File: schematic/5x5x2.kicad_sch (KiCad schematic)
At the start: 180 parts, among them J1 SW Debug, J10 Conn_01x03_Female, J11 Conn_01x03_Male, J12 Conn_01x03_Male, J13 Conn_01x03_Female, J14 Conn_01x03_Female, J15 Conn_01x03_Male, J16 Conn_01x03_Female, J2 USB_C_Receptacle_USB2.0, J3 Conn_01x03_Male, J4 Conn_01x03_Male, J5 Conn_01x03_Female, J6 Conn_01x03_Female, J7 Conn_01x03_Male, J8 Conn_01x03_Male, J9 Conn_01x03_Female, SW1 SW, SW11 SW, SW12 SW, SW13 SW, SW14 SW, SW15 SW, SW21 SW, SW22 SW, SW23 SW, SW24 SW, SW25 SW, SW31 SW, SW32 SW, SW33 SW, SW34 SW, SW35 SW, SW41 SW, SW42 SW, SW43 SW, SW44 SW, SW45 SW, SW51 SW, SW52 SW, SW53 SW, SW54 SW, SW55 SW, SW6 ALPS_EC11, U1 SRV0504, U2 STM32F103C8, U3 LD1117S33CTR, Y1 16M

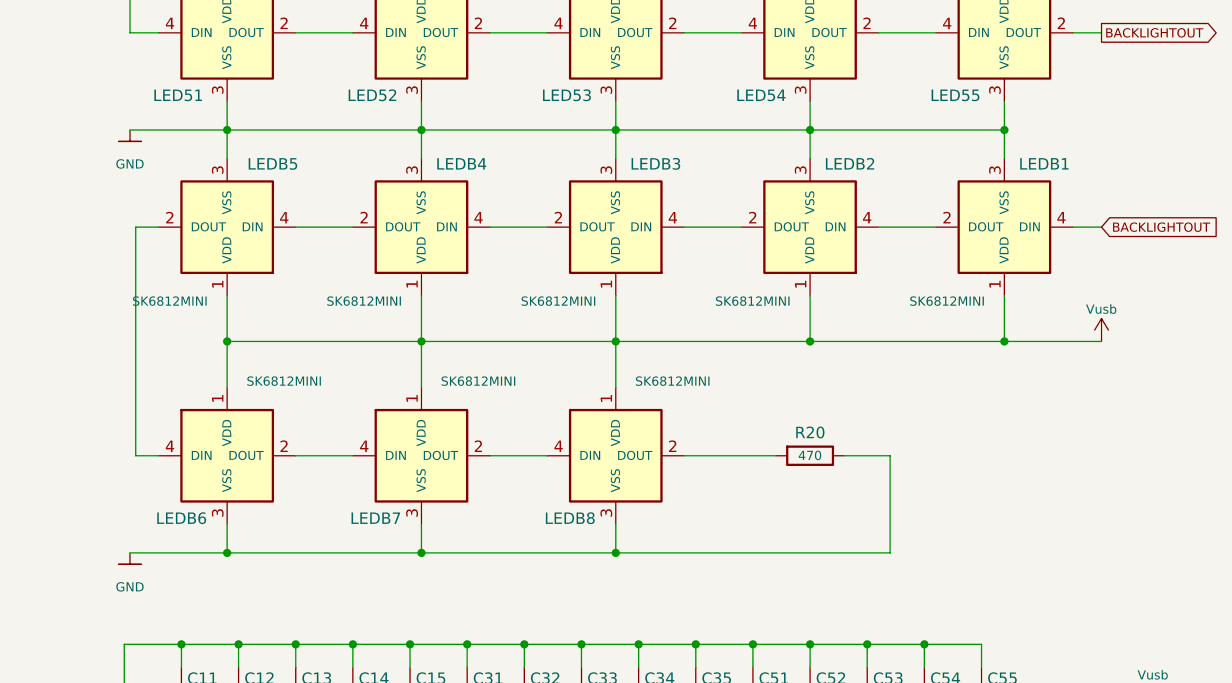
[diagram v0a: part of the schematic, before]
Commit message: Filed for production;
- added a silk voronoi on top of control board
- adjusted wrong footprints for background leds
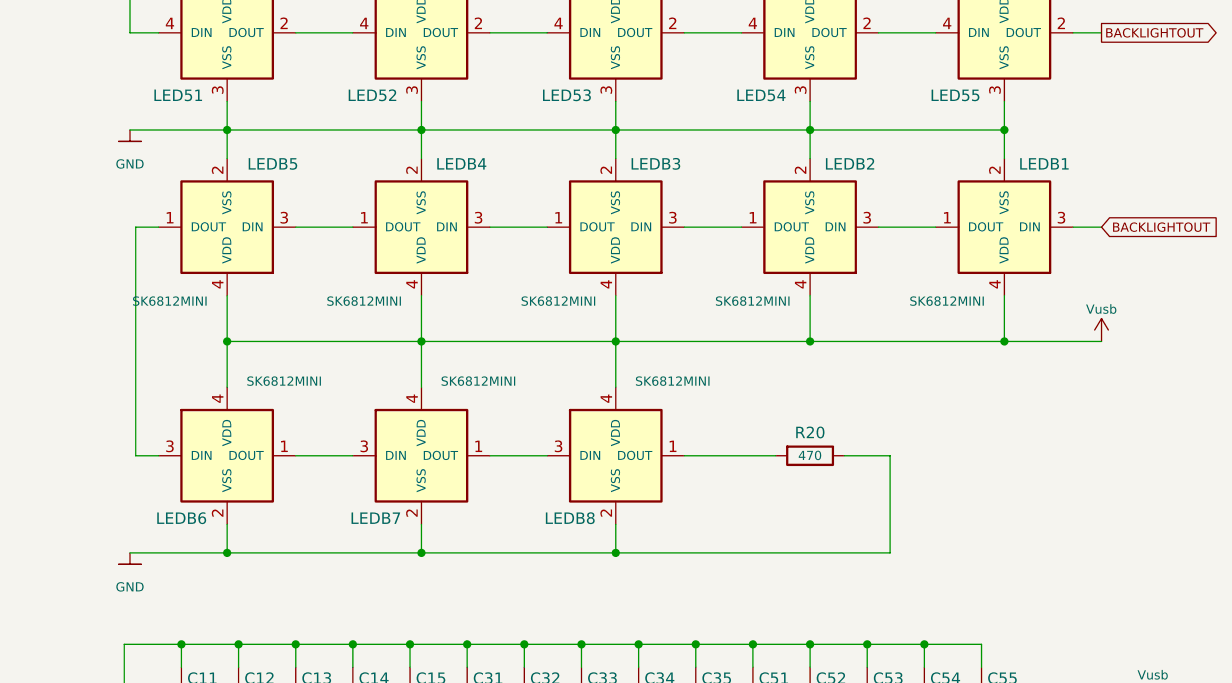
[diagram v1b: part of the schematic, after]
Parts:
- LEDB1, LEDB2, LEDB3, LEDB4, LEDB5, LEDB6, LEDB7, LEDB8: footprint footprints:SK6812MINI_rev -> footprints:SK6812_mini
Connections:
- net BACKLIGHTOUT: now also LEDB1.3 (DIN); no longer LEDB1.4 (DIN)
- net GND: now also LEDB1.2 (VSS), LEDB2.2 (VSS), LEDB3.2 (VSS), LEDB4.2 (VSS), LEDB5.2 (VSS), LEDB6.2 (VSS), LEDB7.2 (VSS), LEDB8.2 (VSS); no longer LEDB1.3 (VSS), LEDB2.3 (VSS), LEDB3.3 (VSS), LEDB4.3 (VSS), LEDB5.3 (VSS), LEDB6.3 (VSS), LEDB7.3 (VSS), LEDB8.3 (VSS)
- net Vusb: now also LEDB1.4 (VDD), LEDB2.4 (VDD), LEDB3.4 (VDD), LEDB4.4 (VDD), LEDB5.4 (VDD), LEDB6.4 (VDD), LEDB7.4 (VDD), LEDB8.4 (VDD); no longer LEDB1.1 (VDD), LEDB2.1 (VDD), LEDB3.1 (VDD), LEDB4.1 (VDD), LEDB5.1 (VDD), LEDB6.1 (VDD), LEDB7.1 (VDD), LEDB8.1 (VDD)
- net at R20.2: now also LEDB8.1 (DOUT); no longer LEDB8.2 (DOUT)
- new net: LEDB7.1 (DOUT), LEDB8.3 (DIN)
- new net: LEDB6.1 (DOUT), LEDB7.3 (DIN)
- new net: LEDB5.1 (DOUT), LEDB6.3 (DIN)
- new net: LEDB1.1 (DOUT), LEDB2.3 (DIN)
- new net: LEDB3.1 (DOUT), LEDB4.3 (DIN)
- new net: LEDB2.1 (DOUT), LEDB3.3 (DIN)
- new net: LEDB4.1 (DOUT), LEDB5.3 (DIN)
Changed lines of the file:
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@@
       (effects (font (size 1.016 1.016)))
     )
-    (property "Footprint" "footprints:SK6812MINI_rev" (id 2) (at 334.645 173.99 0)
+    (property "Footprint" "footprints:SK6812_mini" (id 2) (at 334.645 173.99 0)
       (effects (font (size 1.27 1.27)) hide)
     )
@@
     (pin "1")
   )
-  (symbol (lib_id "SK68xx:SK6812MINI") (at 288.925 167.64 0) (unit 1)
+  (symbol (lib_name "SK6812MINI_2") (lib_id "SK68xx:SK6812MINI") (at 288.925 167.64 0) (unit 1)
     (in_bom yes) (on_board yes)
     (property "Reference" "LEDB6" (id 0) (at 283.845 174.625 0))
@@
       (effects (font (size 1.016 1.016)))
     )
-    (property "Footprint" "footprints:SK6812MINI_rev" (id 2) (at 291.465 173.99 0)
+    (property "Footprint" "footprints:SK6812_mini" (id 2) (at 291.465 173.99 0)
       (effects (font (size 1.27 1.27)) hide)
     )
@@
     (pin "2")
   )
-  (symbol (lib_id "SK68xx:SK6812MINI") (at 375.285 142.24 180) (unit 1)
+  (symbol (lib_name "SK6812MINI_1") (lib_id "SK68xx:SK6812MINI") (at 375.285 142.24 180) (unit 1)
     (in_bom yes) (on_board yes)
     (property "Reference" "LEDB1" (id 0) (at 379.73 135.255 0))
@@
       (effects (font (size 1.016 1.016)))
     )
-    (property "Footprint" "footprints:SK6812MINI_rev" (id 2) (at 372.745 135.89 0)
+    (property "Footprint" "footprints:SK6812_mini" (id 2) (at 372.745 135.89 0)
       (effects (font (size 1.27 1.27)) hide)
     )
@@
     (pin "4")
   )
-  (symbol (lib_id "SK68xx:SK6812MINI") (at 332.105 142.24 180) (unit 1)
+  (symbol (lib_name "SK6812MINI_6") (lib_id "SK68xx:SK6812MINI") (at 332.105 142.24 180) (unit 1)
     (in_bom yes) (on_board yes)
     (property "Reference" "LEDB3" (id 0) (at 336.55 135.255 0))
@@
       (effects (font (size 1.016 1.016)))
     )
-    (property "Footprint" "footprints:SK6812MINI_rev" (id 2) (at 329.565 135.89 0)
+    (property "Footprint" "footprints:SK6812_mini" (id 2) (at 329.565 135.89 0)
       (effects (font (size 1.27 1.27)) hide)
     )
@@
     (pin "2")
   )
-  (symbol (lib_id "SK68xx:SK6812MINI") (at 288.925 142.24 180) (unit 1)
+  (symbol (lib_name "SK6812MINI_5") (lib_id "SK68xx:SK6812MINI") (at 288.925 142.24 180) (unit 1)
     (in_bom yes) (on_board yes)
     (property "Reference" "LEDB5" (id 0) (at 294.005 135.255 0))
@@
       (effects (font (size 1.016 1.016)))
     )
-    (property "Footprint" "footprints:SK6812MINI_rev" (id 2) (at 286.385 135.89 0)
+    (property "Footprint" "footprints:SK6812_mini" (id 2) (at 286.385 135.89 0)
       (effects (font (size 1.27 1.27)) hide)
     )
@@
     (pin "2")
   )
-  (symbol (lib_id "SK68xx:SK6812MINI") (at 310.515 167.64 0) (unit 1)
+  (symbol (lib_name "SK6812MINI_3") (lib_id "SK68xx:SK6812MINI") (at 310.515 167.64 0) (unit 1)
     (in_bom yes) (on_board yes)
     (property "Reference" "LEDB7" (id 0) (at 305.435 174.625 0))
@@
       (effects (font (size 1.016 1.016)))
     )
-    (property "Footprint" "footprints:SK6812MINI_rev" (id 2) (at 313.055 173.99 0)
+    (property "Footprint" "footprints:SK6812_mini" (id 2) (at 313.055 173.99 0)
       (effects (font (size 1.27 1.27)) hide)
     )
@@
     (pin "2")
   )
-  (symbol (lib_id "SK68xx:SK6812MINI") (at 353.695 142.24 180) (unit 1)
+  (symbol (lib_name "SK6812MINI_7") (lib_id "SK68xx:SK6812MINI") (at 353.695 142.24 180) (unit 1)
     (in_bom yes) (on_board yes)
     (property "Reference" "LEDB2" (id 0) (at 358.14 135.255 0))
@@
       (effects (font (size 1.016 1.016)))
     )
-    (property "Footprint" "footprints:SK6812MINI_rev" (id 2) (at 351.155 135.89 0)
+    (property "Footprint" "footprints:SK6812_mini" (id 2) (at 351.155 135.89 0)
       (effects (font (size 1.27 1.27)) hide)
     )
@@
     (pin "2")
   )
-  (symbol (lib_id "SK68xx:SK6812MINI") (at 310.515 142.24 180) (unit 1)
+  (symbol (lib_name "SK6812MINI_4") (lib_id "SK68xx:SK6812MINI") (at 310.515 142.24 180) (unit 1)
     (in_bom yes) (on_board yes)
     (property "Reference" "LEDB4" (id 0) (at 314.96 135.255 0))
@@
       (effects (font (size 1.016 1.016)))
     )
-    (property "Footprint" "footprints:SK6812MINI_rev" (id 2) (at 307.975 135.89 0)
+    (property "Footprint" "footprints:SK6812_mini" (id 2) (at 307.975 135.89 0)
       (effects (font (size 1.27 1.27)) hide)
     )
@@
     )
     (path "/24ee694a-ff65-4bbb-b24d-165de332ba43"
-      (reference "LEDB1") (unit 1) (value "SK6812MINI") (footprint "footprints:SK6812MINI_rev")
+      (reference "LEDB1") (unit 1) (value "SK6812MINI") (footprint "footprints:SK6812_mini")
     )
     (path "/bac0df77-a95c-46b8-9011-d6db9cfd6314"
-      (reference "LEDB2") (unit 1) (value "SK6812MINI") (footprint "footprints:SK6812MINI_rev")
+      (reference "LEDB2") (unit 1) (value "SK6812MINI") (footprint "footprints:SK6812_mini")
     )
     (path "/70fb63e2-79af-42cb-9064-d8eaa0647526"
-      (reference "LEDB3") (unit 1) (value "SK6812MINI") (footprint "footprints:SK6812MINI_rev")
+      (reference "LEDB3") (unit 1) (value "SK6812MINI") (footprint "footprints:SK6812_mini")
     )
     (path "/edda0cc1-81a2-4a7d-8d9a-68a2225d7e2f"
-      (reference "LEDB4") (unit 1) (value "SK6812MINI") (footprint "footprints:SK6812MINI_rev")
+      (reference "LEDB4") (unit 1) (value "SK6812MINI") (footprint "footprints:SK6812_mini")
     )
     (path "/81f00005-5a37-4b7e-b030-6da07af882bb"
-      (reference "LEDB5") (unit 1) (value "SK6812MINI") (footprint "footprints:SK6812MINI_rev")
+      (reference "LEDB5") (unit 1) (value "SK6812MINI") (footprint "footprints:SK6812_mini")
     )
     (path "/24b8356b-294d-404c-8666-483fb1eaf2f6"
-      (reference "LEDB6") (unit 1) (value "SK6812MINI") (footprint "footprints:SK6812MINI_rev")
+      (reference "LEDB6") (unit 1) (value "SK6812MINI") (footprint "footprints:SK6812_mini")
     )
     (path "/a732df08-5b35-43a2-9369-53462d72c67b"
-      (reference "LEDB7") (unit 1) (value "SK6812MINI") (footprint "footprints:SK6812MINI_rev")
+      (reference "LEDB7") (unit 1) (value "SK6812MINI") (footprint "footprints:SK6812_mini")
     )
     (path "/183faf54-e3b0-4e7d-9837-90681c8919c6"
-      (reference "LEDB8") (unit 1) (value "SK6812MINI") (footprint "footprints:SK6812MINI_rev")
+      (reference "LEDB8") (unit 1) (value "SK6812MINI") (footprint "footprints:SK6812_mini")
     )
     (path "/40f32b60-0046-46a8-b8cc-8bddae0d7652"
